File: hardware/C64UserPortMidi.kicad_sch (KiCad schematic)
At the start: 15 parts

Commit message: New hardware design update. Version 1.0 Revision A.
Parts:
- removed C3: (no value), symbol Device:C
- removed U1: (no value), symbol C64UserPortMidi-rescue:ATtiny13A-PU-MCU_Microchip_ATtiny
- removed U3: (no value), symbol 74xx:74HC595
- added C3: 0.1uF, Capacitor_THT:CP_Radial_D5.0mm_P2.00mm, symbol C64UserPortMidi-rescue:CP-Device
- added C4: 10uF, Capacitor_THT:CP_Radial_D5.0mm_P2.00mm, symbol C64UserPortMidi-rescue:CP-Device
- added J4: MIDI OUT, Video Connectors:din-5, symbol hackup-commodore:DIN-5
- added JP1: MIDI Output Bypass, Jumper:SolderJumper-2_P1.3mm_Open_RoundedPad1.0x1.5mm, symbol Jumper:Jumper_2_Open
- added JP2: RST Bypass, Jumper:SolderJumper-2_P1.3mm_Bridged_RoundedPad1.0x1.5mm, symbol Jumper:Jumper_2_Bridged
- added Q1: 2N3904, Package_TO_SOT_THT:TO-92_Inline, symbol Transistor_BJT:2N3904
- added R5, R6: 220, Resistor_THT:R_Axial_DIN0207_L6.3mm_D2.5mm_P7.62mm_Horizontal, symbol Device:R
- added R7: 10k, Resistor_THT:R_Axial_DIN0207_L6.3mm_D2.5mm_P7.62mm_Horizontal, symbol Device:R
- added TP1: PD4, TestPoint:TestPoint_THTPad_D1.5mm_Drill0.7mm, symbol Connector:TestPoint
- added TP3: PD6, TestPoint:TestPoint_THTPad_D1.5mm_Drill0.7mm, symbol Connector:TestPoint
- added TP4: PA2, TestPoint:TestPoint_THTPad_D1.5mm_Drill0.7mm, symbol Connector:TestPoint
- added U1: ATtiny2313-20P, Package_DIP:DIP-20_W7.62mm_Socket_LongPads, symbol MCU_Microchip_ATtiny:ATtiny2313-20P
- C1, C2: value (none) -> 0.1uF; footprint (none) -> Capacitor_THT:CP_Radial_D5.0mm_P2.00mm
- D1: value (none) -> 1N914; footprint (none) -> Diode_THT:D_DO-35_SOD27_P7.62mm_Horizontal
- D2: value (none) -> LED; footprint (none) -> LED_THT:LED_D3.0mm
- J1: value (none) -> C64-UserPort; footprint (none) -> Commodore64C:Connector_Edge_2x12_P3.96mm
- J2: value (none) -> MIDI IN; footprint (none) -> Video Connectors:din-5
- J3: value (none) -> AVR-ISP-6; footprint (none) -> Connector_PinHeader_2.54mm:PinHeader_2x03_P2.54mm_Vertical
- R1, R2, R4: value (none) -> 220; footprint (none) -> Resistor_THT:R_Axial_DIN0207_L6.3mm_D2.5mm_P7.62mm_Horizontal
- R3: value (none) -> 4.7k; footprint (none) -> Resistor_THT:R_Axial_DIN0207_L6.3mm_D2.5mm_P7.62mm_Horizontal
- U2: value (none) -> 6N138; footprint (none) -> Package_DIP:DIP-8_W7.62mm_Socket_LongPads
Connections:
- net D0: now also U1.12 (PB0)
- net D1: now also U1.13 (PB1)
- net D2: now also U1.14 (PB2)
- net D3: now also U1.15 (PB3)
- net D4: now also U1.16 (PB4)
- net GND: now also U2.1 (NC), U2.4 (NC), C3.2, C4.2, J4.2, Q1.1 (E), U1.10 (GND)
- net LATCH: now also U1.9 (PD5)
- net RECV: now also U1.6 (PD2); no longer J3.3 (SCK)
- net RX: now also U1.2 (PD0); no longer J3.4 (MOSI)
- net VCC: now also C3.1, C4.1, R6.2, U1.20 (VCC); no longer C2.1
- net ~{RST}: now also JP2.2 (B), U1.1 (PA2/~{RESET}); no longer J1.3 (/RST)
- net at J1.M (PA2): now also TP4.1
- net at J2.2: now also C2.1
- net D5 renamed MOSI
- net MOSI: now also J3.4 (MOSI), U1.17 (PB5)
- net D6 renamed MISO
- net MISO: now also J3.1 (MISO), U1.18 (PB6)
- net D7 renamed SCK
- net SCK: now also J3.3 (SCK), U1.19 (PB7)
- net DATA: no longer names the net of D2.2 (A)
- net DATA: now also U1.7 (PD3); no longer J3.1 (MISO)
- new net: J1.3 (/RST), JP2.1 (A)
- new net: TP3.1, U1.11 (PD6)
- new net: TP1.1, U1.8 (PD4)
- new net: Q1.2 (B), R7.1
- new net: JP1.2 (B), Q1.3 (C), R5.2
- new net: J4.4, R6.1
- new net: J4.5, R5.1
- new net TX: JP1.1 (A), R7.2, U1.3 (PD1)
- no-connect marks 0 -> 2
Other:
- note added: "MIDI Output"
- note added: "Or 2n2222, 2n5551."
- note added: "Unused pins used as ground plane ties."
- note added: "User Port"
- note removed: "User Port Data Register"
- company: (none) -> D Cooper Dalrymple
- title: (none) -> C64UserPortMidi
- moved on the sheet: C1, D1, J1, J2, J3, R1, R2, R3, U2

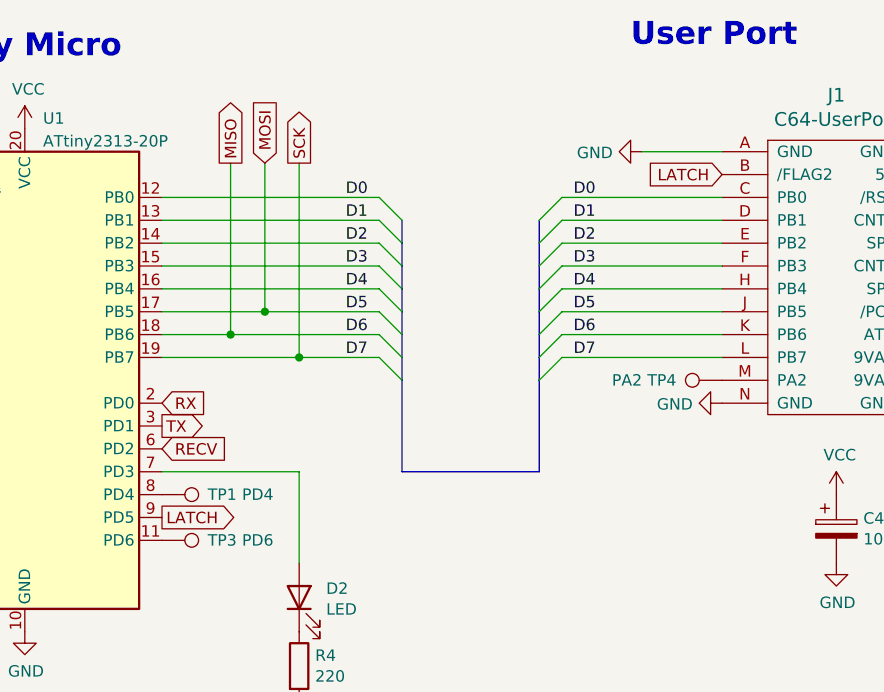
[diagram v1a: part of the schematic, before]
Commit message: Rename latch to flag in schematic.
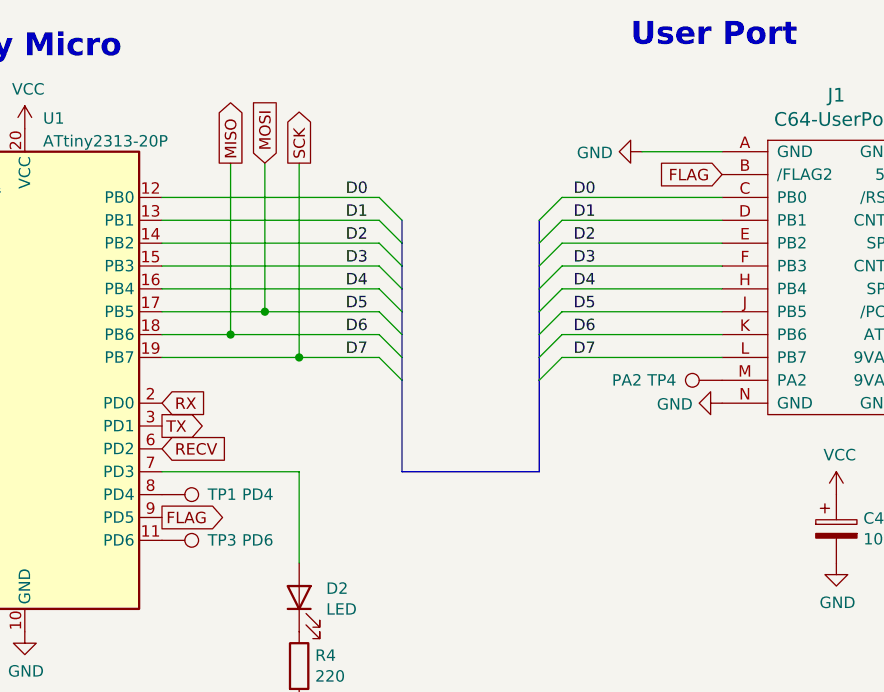
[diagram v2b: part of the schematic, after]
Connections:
- net LATCH renamed FLAG
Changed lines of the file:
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@@
     )
   )
-  (global_label "LATCH" (shape input) (at 214.63 92.71 180) (fields_autoplaced)
+  (global_label "FLAG" (shape input) (at 214.63 92.71 180) (fields_autoplaced)
     (effects (font (size 1.27 1.27)) (justify right))
-    (property "Intersheet References" "${INTERSHEET_REFS}" (id 0) (at -1.27 36.83 0)
-      (effects (font (size 1.27 1.27)) hide)
+    (property "Intersheet References" "${INTERSHEET_REFS}" (id 0) (at 207.8306 92.6306 0)
+      (effects (font (size 1.27 1.27)) (justify right) hide)
     )
   )
@@
     )
   )
-  (global_label "LATCH" (shape output) (at 152.4 130.81 0) (fields_autoplaced)
+  (global_label "FLAG" (shape output) (at 152.4 130.81 0) (fields_autoplaced)
     (effects (font (size 1.27 1.27)) (justify left))
-    (property "Intersheet References" "${INTERSHEET_REFS}" (id 0) (at 73.66 -22.86 0)
-      (effects (font (size 1.27 1.27)) hide)
+    (property "Intersheet References" "${INTERSHEET_REFS}" (id 0) (at 159.1994 130.7306 0)
+      (effects (font (size 1.27 1.27)) (justify left) hide)
     )
   )

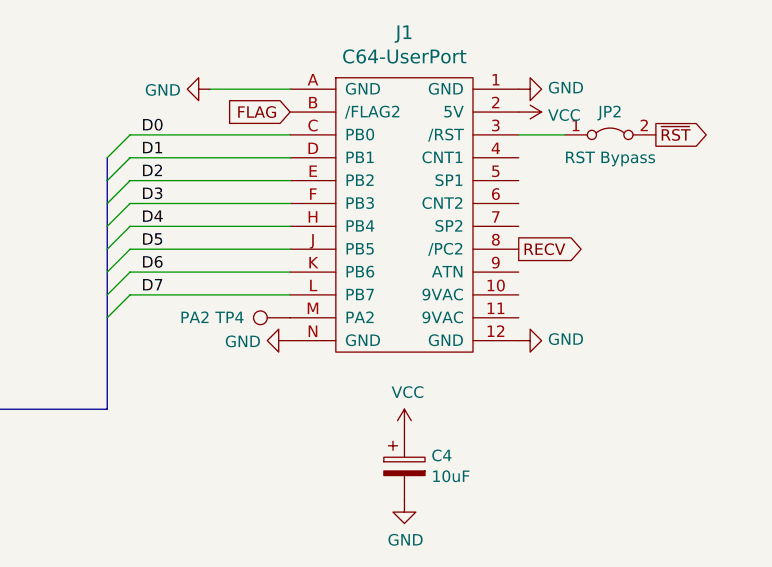
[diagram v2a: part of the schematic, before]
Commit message: Fixed PA2 error in schematic, rerouted traces, and regenerated gerber files.
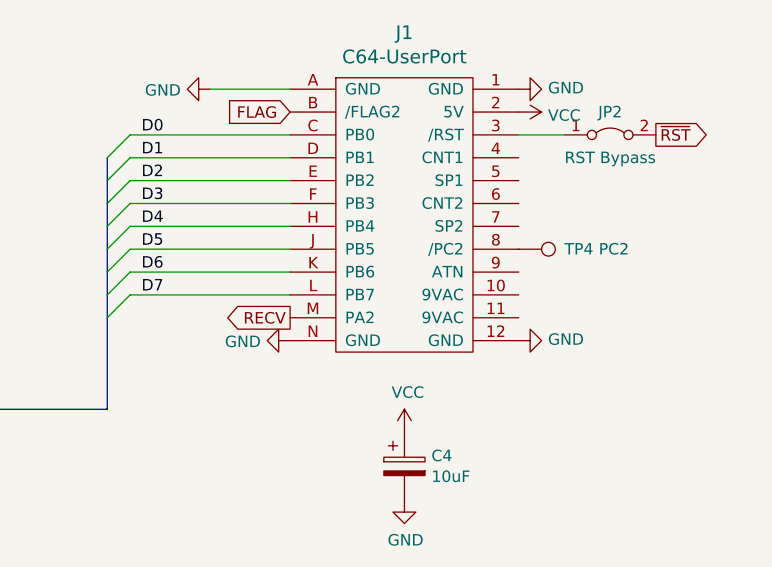
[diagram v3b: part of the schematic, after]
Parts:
- TP4: value PA2 -> PC2
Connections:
- net RECV: now also J1.M (PA2); no longer J1.8 (/PC2)
- net at TP4.1: now also J1.8 (/PC2); no longer J1.M (PA2)
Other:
- moved on the sheet: TP4
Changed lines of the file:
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@@
   (title_block
     (title "C64UserPortMidi")
-    (date "2022-12-11")
-    (rev "v1.0 RevA")
+    (date "2023-01-03")
+    (rev "v1.0 RevB")
     (company "D Cooper Dalrymple")
     (comment 1 "https://dcdalrymple.com/C64UserPortMidi")
@@
     )
   )
-  (global_label "RECV" (shape output) (at 240.03 107.95 0) (fields_autoplaced)
-    (effects (font (size 1.27 1.27)) (justify left))
-    (property "Intersheet References" "${INTERSHEET_REFS}" (id 0) (at -1.27 36.83 0)
+  (global_label "RECV" (shape output) (at 214.63 115.57 180) (fields_autoplaced)
+    (effects (font (size 1.27 1.27)) (justify right))
+    (property "Intersheet References" "${INTERSHEET_REFS}" (id 0) (at 455.93 186.69 0)
       (effects (font (size 1.27 1.27)) hide)
     )
@@
     (pin "1")
   )
-  (symbol (lib_id "Connector:TestPoint") (at 214.63 115.57 90) (unit 1)
-    (in_bom yes) (on_board yes)
-    (property "Reference" "TP4" (id 0) (at 209.55 115.57 90)
-      (effects (font (size 1.27 1.27)) (justify left))
-    )
-    (property "Value" "PA2" (id 1) (at 205.74 115.57 90)
-      (effects (font (size 1.27 1.27)) (justify left))
-    )
-    (property "Footprint" "TestPoint:TestPoint_THTPad_D1.5mm_Drill0.7mm" (id 2) (at 214.63 110.49 0)
-      (effects (font (size 1.27 1.27)) hide)
-    )
-    (property "Datasheet" "~" (id 3) (at 214.63 110.49 0)
+  (symbol (lib_id "Connector:TestPoint") (at 240.03 107.95 270) (unit 1)
+    (in_bom yes) (on_board yes)
+    (property "Reference" "TP4" (id 0) (at 245.11 107.95 90)
+      (effects (font (size 1.27 1.27)) (justify left))
+    )
+    (property "Value" "PC2" (id 1) (at 248.92 107.95 90)
+      (effects (font (size 1.27 1.27)) (justify left))
+    )
+    (property "Footprint" "TestPoint:TestPoint_THTPad_D1.5mm_Drill0.7mm" (id 2) (at 240.03 113.03 0)
+      (effects (font (size 1.27 1.27)) hide)
+    )
+    (property "Datasheet" "~" (id 3) (at 240.03 113.03 0)
       (effects (font (size 1.27 1.27)) hide)
     )
@@
     )
     (path "/2c056867-6594-4364-9fb3-9c4bf8c74d75"
-      (reference "TP4") (unit 1) (value "PA2") (footprint "TestPoint:TestPoint_THTPad_D1.5mm_Drill0.7mm")
+      (reference "TP4") (unit 1) (value "PC2") (footprint "TestPoint:TestPoint_THTPad_D1.5mm_Drill0.7mm")
     )
     (path "/120c11a0-883d-492d-8f0b-bdde364f6160"
